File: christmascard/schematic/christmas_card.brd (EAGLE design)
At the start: 50 x 50 mm, 85 parts, among them IC1 WS2811-SOP8, IC2 WS2811-SOP8, IC4 LM1117, IC5 WS2811-SOP8, IC6 MEGA8-AI, Q1 MOSFET-NCHANNELSMD, Q10 TRANSISTOR_PNPSMD, Q11 TRANSISTOR_PNPSMD, Q12 TRANSISTOR_PNPSMD, Q2 MOSFET-NCHANNELSMD, Q3 MOSFET-NCHANNELSMD, Q4 MOSFET-NCHANNELSMD, Q5 TRANSISTOR_PNPSMD, Q9 TRANSISTOR_PNPSMD, X2 USB-MICROB

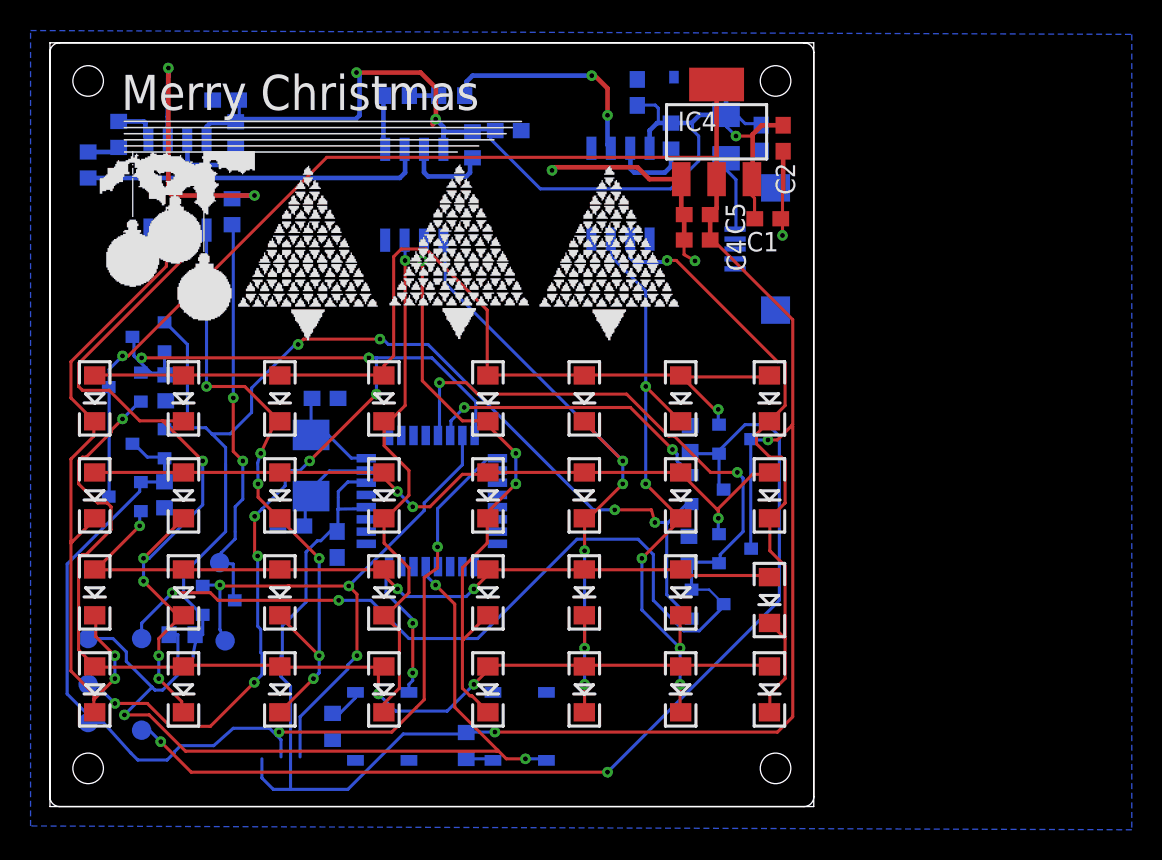
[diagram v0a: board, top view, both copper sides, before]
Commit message: Relocated files, removed unused files, updated christmas and clock board and other changes
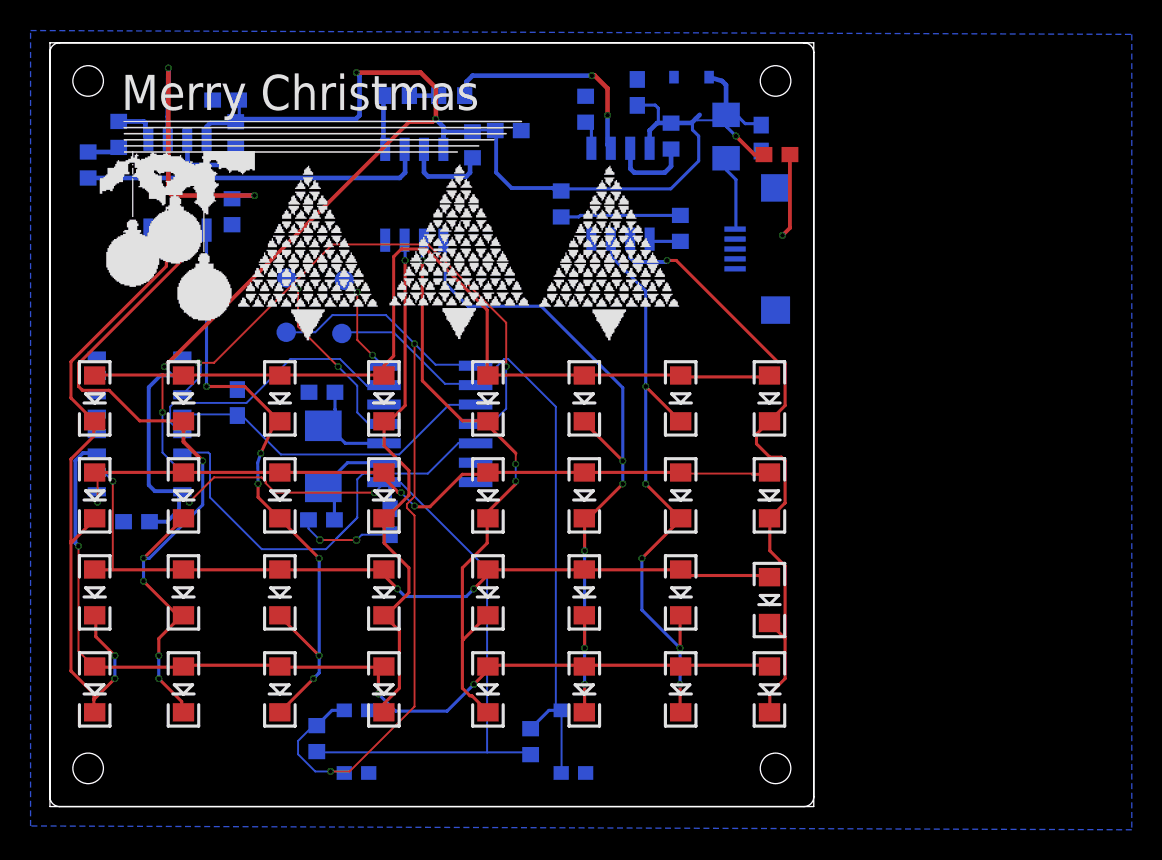
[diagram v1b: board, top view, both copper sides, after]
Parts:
- removed C2, C4: 100nF, adafruit:C0603
- removed C5: 10nF, adafruit:C0603
- removed IC4: LM1117, voltage_regulators:SOT223
- removed IC6: MEGA8-AI, atmel:TQFP32-08
- removed Q1, Q2, Q3, Q4: MOSFET-NCHANNELSMD, SparkFun:SOT23-3
- removed Q10, Q11, Q12, Q5, Q9: TRANSISTOR_PNPSMD, SparkFun:SOT23-3
- removed R14: 10K, adafruit:R0603
- removed R15: 1K, adafruit:R0603
- removed R4: (no value), adafruit:R0603
- removed S1, S2: SWITCH-MOMENTARY-2SMD-2, SparkFun:TACTILE_SWITCH_SMD-2
- removed TP3, TP5, TP6: TPB1,27, testpad:B1,27
- added C12: 100nF, adafruit:C0603
- added C13: 10nF, adafruit:C0603
- added IC7: 74LS595D, SparkFun:SO16
- added R16: 33, adafruit:R0603
- added S3, S4: MOMENTARY-SWITCH-SPST-SMD-4.6X2.8MM, SparkFun-Switches:TACTILE_SWITCH_SMD_4.6X2.8MM
- added U3: ATTINY24/44/84-SSU, bt_avr:SOIC14N
- R13: value 10K -> 33
- R5: value (none) -> 33
- moved R13 36.0 mm to (33.6, 39.4), turned to 270 degrees
- moved R5 35.3 mm to (41.4, 37.8), turned to 270 degrees
- moved R3 27.3 mm to (17.6, 4.40)
- moved TP1 26.9 mm to (15.6, 34.6)
- moved TP2 26.4 mm to (15.6, 31.0)
- moved TP4 24.9 mm to (19.4, 34.4)
- moved R2 22.4 mm to (31.6, 4.20)
- moved TP7 17.0 mm to (19.2, 30.9)
- moved C1 4.24 mm to (47.7, 42.6)
- moved C6 3.77 mm to (22.4, 18.6), turned to 270 degrees
- moved C10 2.04 mm to (17.9, 18.7)
- moved X1 1.00 mm to (18.0, 22.9)
- moved C11 0.45 mm to (17.9, 27.1), turned to 180 degrees
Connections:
- removed net 3.3V: C4.1, C5.1, C6.2, IC4.2, IC4.4, IC6.4, IC6.6, Q1.3, Q2.3, Q3.3, Q4.3, R13.2
- removed net AVCC: IC6.18
- removed net MOSFET_STATUS: Q10.1, Q11.1, Q12.1, Q5.1, Q9.1, R15.2
- removed net N$13: Q3.1, Q9.3, R2.2
- removed net N$9: R13.1, S1.1
- removed net ROW0: IC6.14, Q9.2, TP6.TP
- removed net ROW1: IC6.13, Q1.1, Q10.2, Q10.3, R3.2, TP5.TP
- removed net ROW2: IC6.17, Q11.2, Q11.3, Q2.1, R4.2, TP3.TP
- removed net ROW3: IC6.16, Q12.2, Q12.3, Q4.1, R5.2, TP2.TP
- removed net VCC: C1.1, C2.1, C3.1, C7.1, C8.1, C9.1, D1.1, F1.1, IC1.8, IC2.8, IC4.3, IC5.8, R10.1, R11.1, R12.1
- new net 5V: C1.1, C12.1, C3.1, C6.1, C7.1, C8.1, C9.1, D1.1, F1.1, IC1.8, IC2.8, IC5.8, IC7.10, IC7.16, R10.1, R11.1, R12.1, R13.1, R2.2, R3.2, U3.1
- new net BT0: R2.1, S3.3, S3.4, TP7.TP, U3.9
- new net BT1: R3.1, S4.3, S4.4, TP2.TP, U3.8
- new net LATCH: C13.2, IC7.12, U3.10
- new net LEDATA: U3.13
- new net N$16: U3.5
- new net N$40: IC7.9
- new net PWM: IC7.13, U3.6
- new net RCLK: IC7.11, U3.11
- new net SER: IC7.14, U3.12
- net GND: now also C12.2, C13.1, C6.2, IC7.8, S3.1, S3.2, S4.1, S4.2, U3.14; no longer C2.2, C4.2, C5.2, C6.1, IC4.1, IC6.21, IC6.3, IC6.5, R14.1, R2.1, R3.1, R4.1, R5.1
- net LEDDATA: no longer Q5.3, TP7.TP
- net LEDROW0: now also IC7.15; no longer Q3.2
- net LEDROW1: now also IC7.1; no longer Q1.2
- net LEDROW2: now also IC7.2; no longer Q2.2
- net LEDROW3: now also IC7.3; no longer Q4.2
- net MOSI: now also U3.7; no longer IC6.15, Q5.2
- net N$10: now also U3.2; no longer IC6.7
- net N$11: now also IC5.5, R16.2; no longer IC6.32, S2.1
- net N$12: now also R13.2, R5.1; no longer R14.2, S2.2
- net N$14: now also U3.3; no longer IC6.8
- net N$62: now also R5.2
- net RES: now also U3.4; no longer IC6.29, R15.1, S1.2
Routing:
- net 3.3V: track 173.9 -> 0.00 mm, vias 3 -> 0
- net 5V: track 0.00 -> 163.4 mm, vias 0 -> 6
- net ROW1: track 87.6 -> 0.00 mm, vias 4 -> 0
- net ROW0: track 82.9 -> 0.00 mm, vias 4 -> 0
- net VCC: track 77.3 -> 0.00 mm, vias 3 -> 0
- net MOSFET_STATUS: track 77.2 -> 0.00 mm, vias 4 -> 0
- net ROW3: track 70.2 -> 0.00 mm, vias 8 -> 0
- net ROW2: track 69.0 -> 0.00 mm, vias 2 -> 0
- net BT1: track 0.00 -> 54.0 mm, vias 0 -> 2
- net BT0: track 0.00 -> 44.2 mm
- net RES: track 56.7 -> 12.8 mm, vias 3 -> 2
- net RCLK: track 0.00 -> 36.1 mm, vias 0 -> 2
- net MOSI: track 39.4 -> 6.82 mm, vias 3 -> 2
- net SER: track 0.00 -> 29.8 mm
- net LEDDATA: track 26.4 -> 0.00 mm, vias 2 -> 0
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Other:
- board text removed: "MISO"
- board text removed: "MOSI"
- board text removed: "RES"

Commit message: Removed unused files, update board, code and other changes
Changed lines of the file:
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@@
 <drawing>
 <settings>
-<setting alwaysvectorfont="yes"/>
+<setting alwaysvectorfont="no"/>
 <setting keepoldvectorfont="yes"/>
 <setting verticaltext="up"/>
@@
 <polygon width="0.254" layer="16">
 <vertex x="-1.136846875" y="50.751278125"/>
-<vertex x="70.953153125" y="50.501278125"/>
-<vertex x="70.953153125" y="-1.568721875"/>
+<vertex x="51.153153125" y="50.56994375"/>
+<vertex x="51.153153125" y="-1.50005625"/>
 <vertex x="-1.136846875" y="-1.318721875"/>
 </polygon>

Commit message: Improvement and other changes
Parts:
- removed TP1, TP7: TPB1,27, testpad:B1,27
- added 5V, GND: WIREPADSMD2,54-5,08, wirepad:SMD2,54-5,08
- added D2: (no value), SparkFun-LED:LED-0603
- added R4: 480, adafruit:R0603
- added RES, SCK: TPB1,27, testpad:B1,27
- renumbered TP2 to MISO, TP4 to MOSI
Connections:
- removed net N$16: U3.5
- removed net N$41: F1.2, X2.VBUS
- new net DEBUGLED0: D2.A, U3.5
- new net N$9: D2.C, R4.2
- new net VCC: 5V.1, F1.2, X2.VBUS
- net BT0: now also SCK.TP; no longer TP7.TP
- net GND: now also GND.1, R4.1
- net RES: now also RES.TP; no longer TP1.TP
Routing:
- net VCC: track 0.00 -> 25.7 mm
- net DEBUGLED0: track 0.00 -> 11.4 mm, vias 0 -> 2
- net COL4: track 39.8 -> 45.0 mm
- net N$41: track 4.96 -> 0.00 mm
- net LEDROW1: track 49.5 -> 53.9 mm
- net BT0: track 44.2 -> 48.5 mm
- net COL6: track 40.8 -> 44.0 mm
- net COL2: track 42.0 -> 44.9 mm
- net N$9: track 0.00 -> 2.47 mm
- net COL7: track 41.8 -> 44.3 mm
- net COL1: track 49.1 -> 46.8 mm, vias 6 -> 8
- net COL0: track 45.0 -> 47.2 mm
- net RCLK: track 36.1 -> 38.3 mm
- net COL5: track 46.0 -> 47.8 mm
- net SER: track 29.8 -> 28.2 mm
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
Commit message: Improvement, fixes and other changes
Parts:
- moved R4 0.82 mm to (32.6, 19.4)
- moved D2 0.80 mm to (32.6, 23.8)
- moved C7 0.40 mm to (11.6, 46.6)
- moved R6 0.20 mm to (2.43, 42.0)
- moved C8 0.20 mm to (30.3, 44.2)
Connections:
- removed net LEDATA: U3.13
- net LEDDATA: now also U3.13
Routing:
- net LEDDATA: track 0.00 -> 37.3 mm, vias 0 -> 4
- net DEBUGLED0: track 11.4 -> 12.2 mm
- net 5V: track 162.3 -> 163.0 mm
